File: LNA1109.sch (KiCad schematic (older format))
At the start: 25 parts, among them P1 SMA-KIT-1.5MF, U1 SWITCH, U2 SWITCH, U3 LNA, U4 SAW

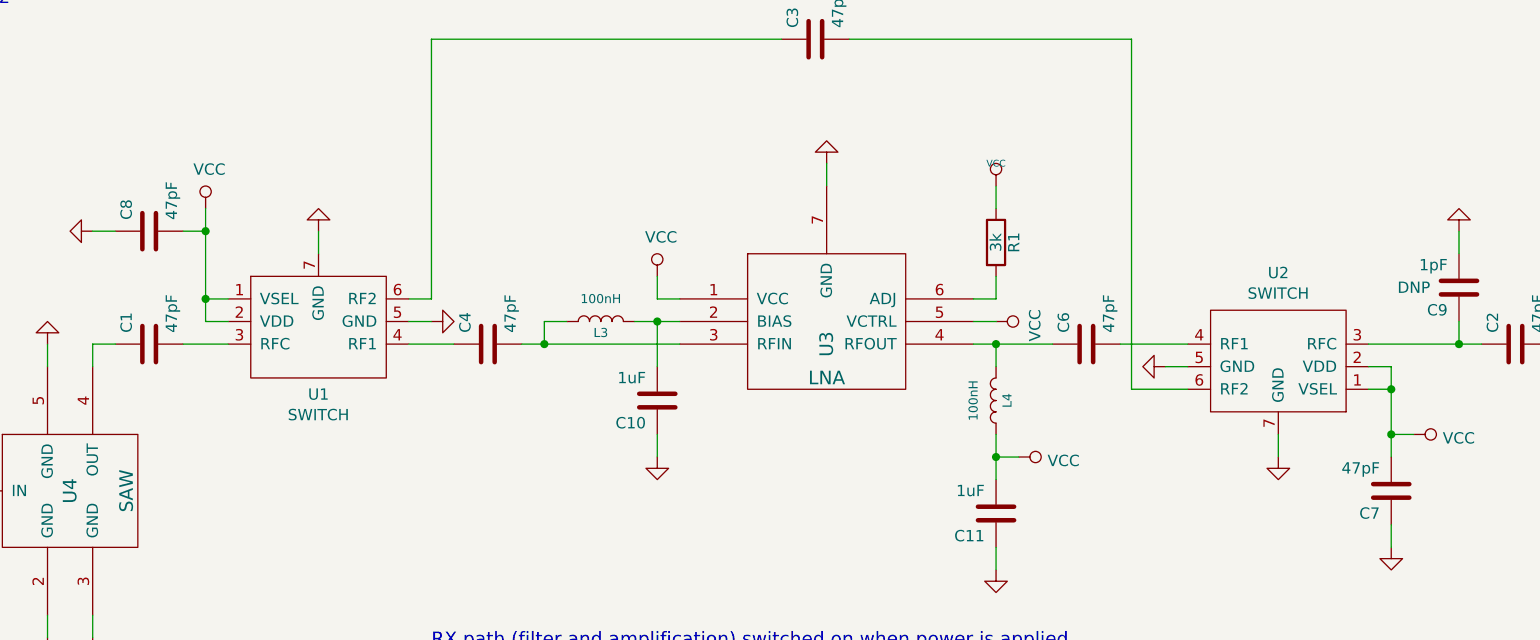
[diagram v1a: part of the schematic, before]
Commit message: correct C7 and C8 part selection
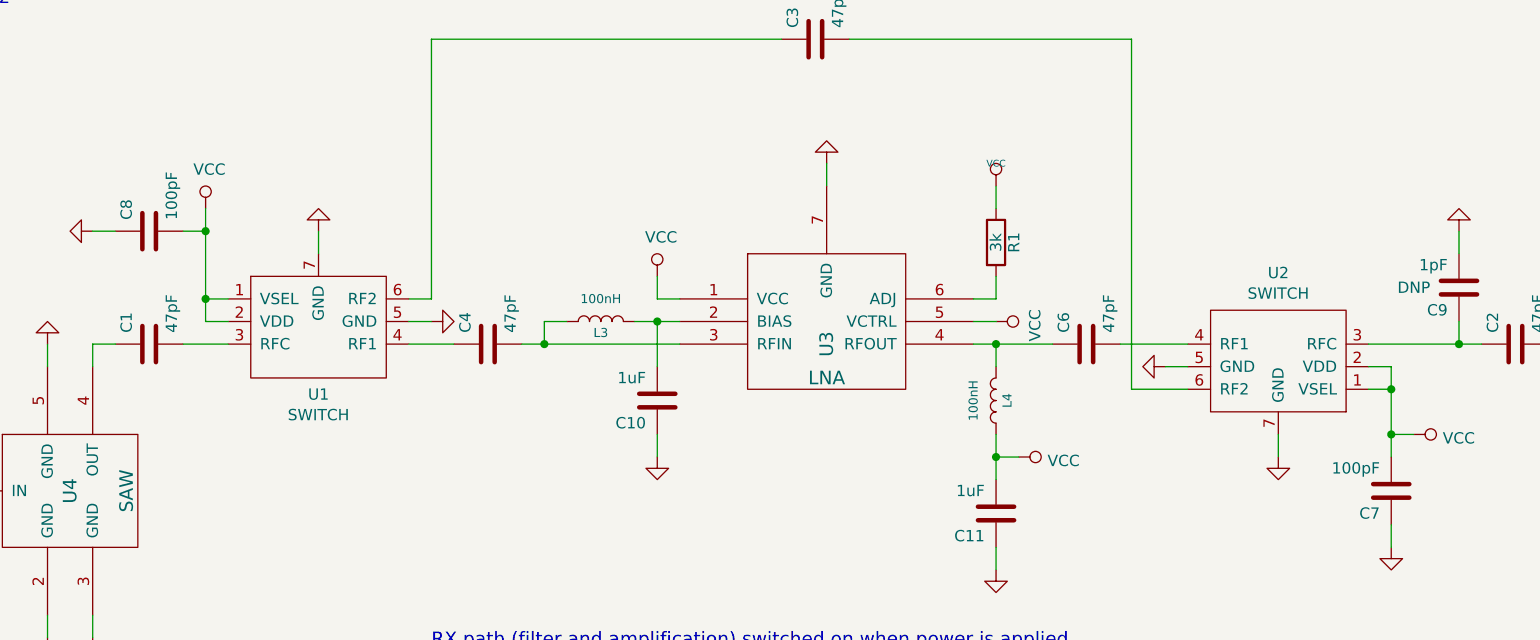
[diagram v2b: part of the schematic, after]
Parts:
- C7, C8: value 47pF -> 100pF; Description CAP CER 47PF 50V C0G/NP0 0402 -> CAP CER 100PF 50V 5% NP0 0402; Part Number GCM1555C1H470JA16D -> GCM1555C1H101JA16D
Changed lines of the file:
@@
 P 3250 2750
 F 0 "C8" H 3300 2850 50  0000 L CNN
-F 1 "47pF" H 3300 2650 50  0000 L CNN
+F 1 "100pF" H 3300 2650 50  0000 L CNN
 F 2 "gsg-modules:0402" H 3250 2750 50  0001 C CNN
 F 3 "" H 3250 2750 50  0001 C CNN
 F 4 "Murata" H 3250 2750 60  0001 C CNN "Manufacturer"
-F 5 "GCM1555C1H470JA16D" H 3250 2750 60  0001 C CNN "Part Number"
-F 6 "CAP CER 47PF 50V C0G/NP0 0402" H 3250 2750 60  0001 C CNN "Description"
+F 5 "GCM1555C1H101JA16D" H 3250 2750 60  0001 C CNN "Part Number"
+F 6 "CAP CER 100PF 50V 5% NP0 0402" H 3250 2750 60  0001 C CNN "Description"
 	1    3250 2750
 	0    -1   -1   0
@@
 P 8750 3900
 F 0 "C7" H 8800 4000 50  0000 L CNN
-F 1 "47pF" H 8800 3800 50  0000 L CNN
+F 1 "100pF" H 8800 3800 50  0000 L CNN
 F 2 "gsg-modules:0402" H 8750 3900 50  0001 C CNN
 F 3 "" H 8750 3900 50  0001 C CNN
 F 4 "Murata" H 8750 3900 60  0001 C CNN "Manufacturer"
-F 5 "GCM1555C1H470JA16D" H 8750 3900 60  0001 C CNN "Part Number"
-F 6 "CAP CER 47PF 50V C0G/NP0 0402" H 8750 3900 60  0001 C CNN "Description"
+F 5 "GCM1555C1H101JA16D" H 8750 3900 60  0001 C CNN "Part Number"
+F 6 "CAP CER 100PF 50V 5% NP0 0402" H 8750 3900 60  0001 C CNN "Description"
 	1    8750 3900
 	-1   0    0    1
